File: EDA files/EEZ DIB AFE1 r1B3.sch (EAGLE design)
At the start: 197 parts, among them IC1 OPA4202IPWR, IC10 N.C., IC11 N.C., IC12 N.C., IC13 ADS131E04IPAGR, IC14 TPS71725DCKR, IC15 TPS72325DBVR, IC2 DG212BDY-T1-E3, IC3 ULN2803ADWR, IC4 OPA4202IPWR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

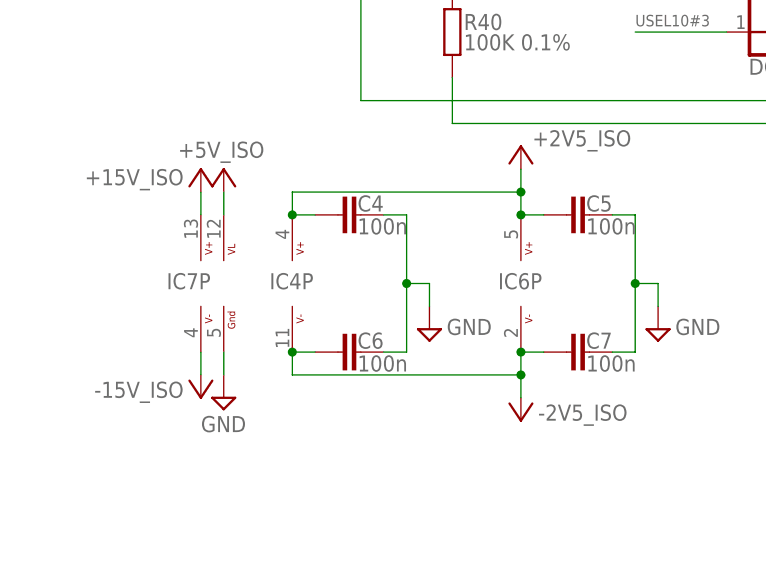
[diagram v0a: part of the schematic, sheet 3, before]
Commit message: PCB silkscreen fix
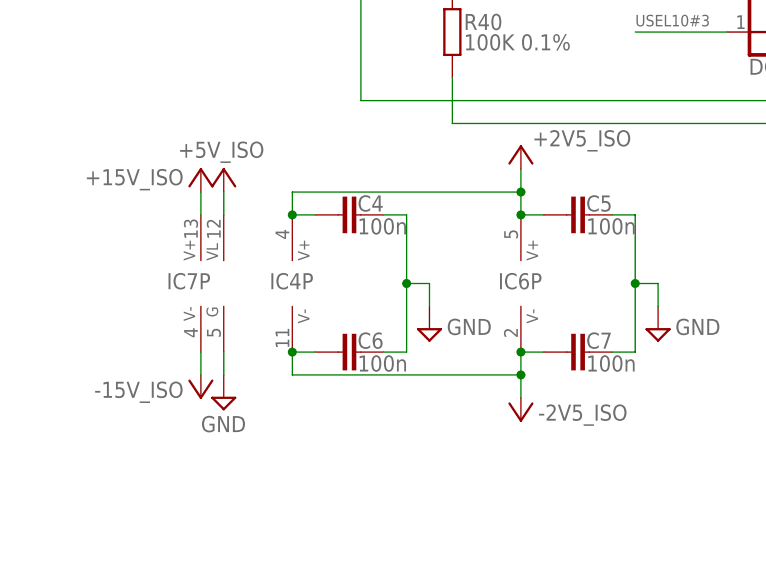
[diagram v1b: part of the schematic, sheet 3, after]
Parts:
- S1: value 2118732-2 -> N.C.
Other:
- moved on the sheet: IC2P, IC5P, IC7P, IC9P
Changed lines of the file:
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@@
 <part name="IC10" library="EEZ_DIB" deviceset="LTC6655" device="BHMS8" value="N.C."/>
 <part name="-2V5_ISO3" library="EEZ_DIB" deviceset="-2V5_ISO" device=""/>
-<part name="S1" library="EEZ_DIB" deviceset="211873" device="2-2"/>
+<part name="S1" library="EEZ_DIB" deviceset="211873" device="2-2" value="N.C."/>
 <part name="SUPPLY25" library="supply2" deviceset="GND" device=""/>
 <part name="L1" library="EEZ_Lib1" deviceset="FERRITE_BEAD" device="0603" value="MLZ1608N100LT000"/>
@@
 </instance>
 <instance part="IC2" gate="P" x="50.8" y="154.94" smashed="yes">
-<attribute name="NAME" x="46.99" y="154.305" size="1.778" layer="95"/>
+<attribute name="NAME" x="48.895" y="154.305" size="1.778" layer="95"/>
 </instance>
 <instance part="IC3" gate="A" x="213.36" y="55.88" smashed="yes">
@@
 <text x="162.56" y="116.84" size="1.778" layer="97" rot="MR180">Isolated +/-2.5 V LDOs</text>
 <rectangle x1="125.73" y1="120.65" x2="255.27" y2="173.99" layer="97"/>
+<rectangle x1="10.16" y1="149.86" x2="30.48" y2="172.72" layer="97"/>
 </plain>
 <instances>

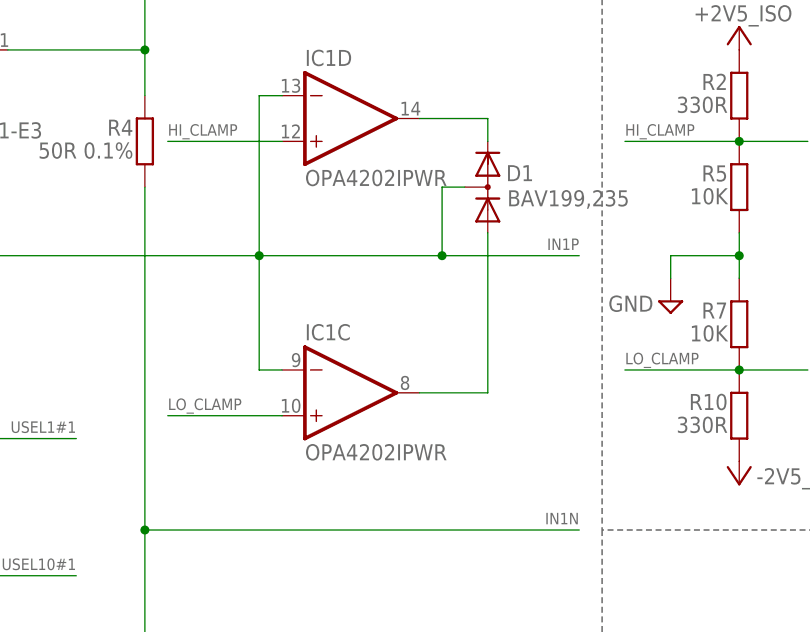
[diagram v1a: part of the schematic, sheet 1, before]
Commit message: active clamp op-amps changed
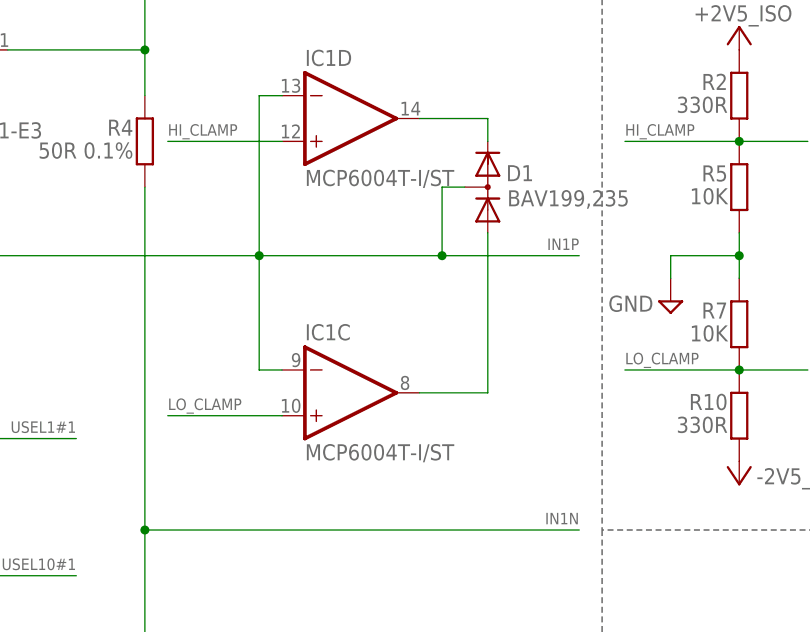
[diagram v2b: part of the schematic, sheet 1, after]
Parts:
- IC1, IC4: value OPA4202IPWR -> MCP6004T-I/ST
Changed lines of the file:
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@@
 <part name="Q1" library="EEZ_Lib1" deviceset="BSP129" device="SOT-223" value="CPC3902ZTR"/>
 <part name="R1" library="rcl" deviceset="R-EU_" device="R0805" value="47R"/>
-<part name="IC1" library="EEZ_TI" deviceset="OPA4197" device="PW" value="OPA4202IPWR"/>
+<part name="IC1" library="EEZ_TI" deviceset="OPA4197" device="PW" value="MCP6004T-I/ST"/>
 <part name="SUPPLY82" library="supply2" deviceset="GND" device=""/>
 <part name="JP3" library="EEZ_Lib1" deviceset="JUMPER-2PIN" device="-2MM" value="DS1025-01-1*2P8BV1-B"/>
@@
 <part name="Q3" library="EEZ_Lib1" deviceset="BSP129" device="SOT-223" value="CPC3902ZTR"/>
 <part name="R18" library="rcl" deviceset="R-EU_" device="R0805" value="47R"/>
-<part name="IC4" library="EEZ_TI" deviceset="OPA4197" device="PW" value="OPA4202IPWR"/>
+<part name="IC4" library="EEZ_TI" deviceset="OPA4197" device="PW" value="MCP6004T-I/ST"/>
 <part name="F2" library="EEZ_Lib1" deviceset="FUSE_RESETTABLE2" device="" value="SN005-60"/>
 <part name="IC5" library="EEZ_DIB" deviceset="DG212B" device="DY-T1-E3" value="DG212BDY-T1-E3"/>
